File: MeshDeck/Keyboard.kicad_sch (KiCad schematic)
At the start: 12 parts, among them U8 RP2040

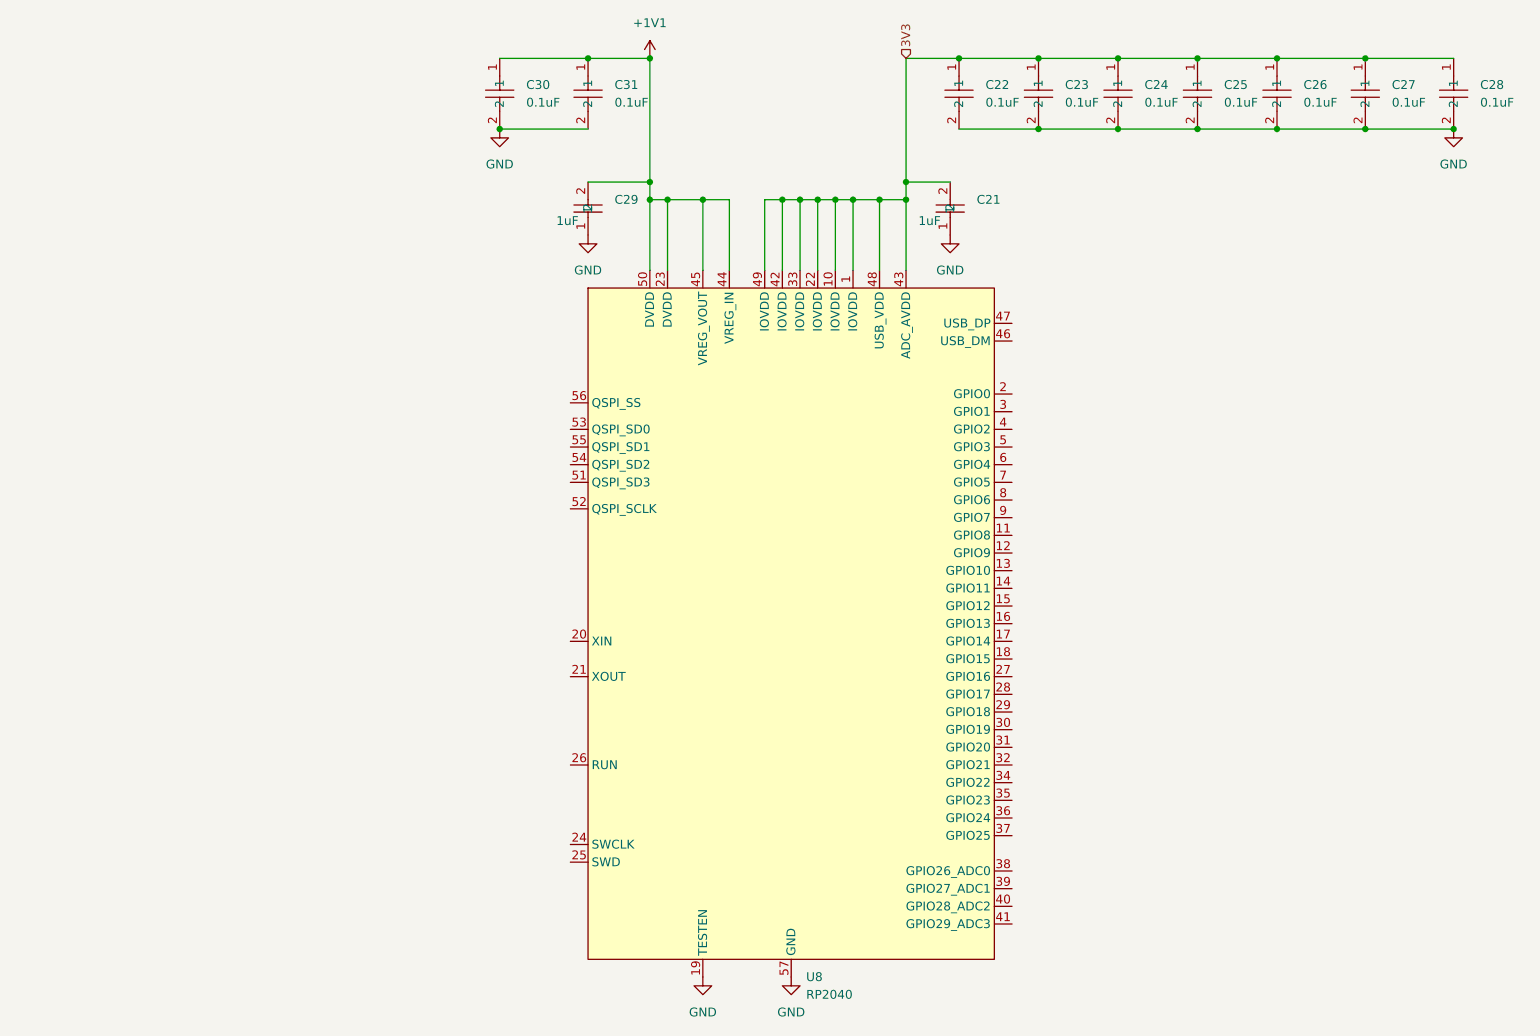
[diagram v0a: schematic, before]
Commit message: started pcb plus pin socket for expansion
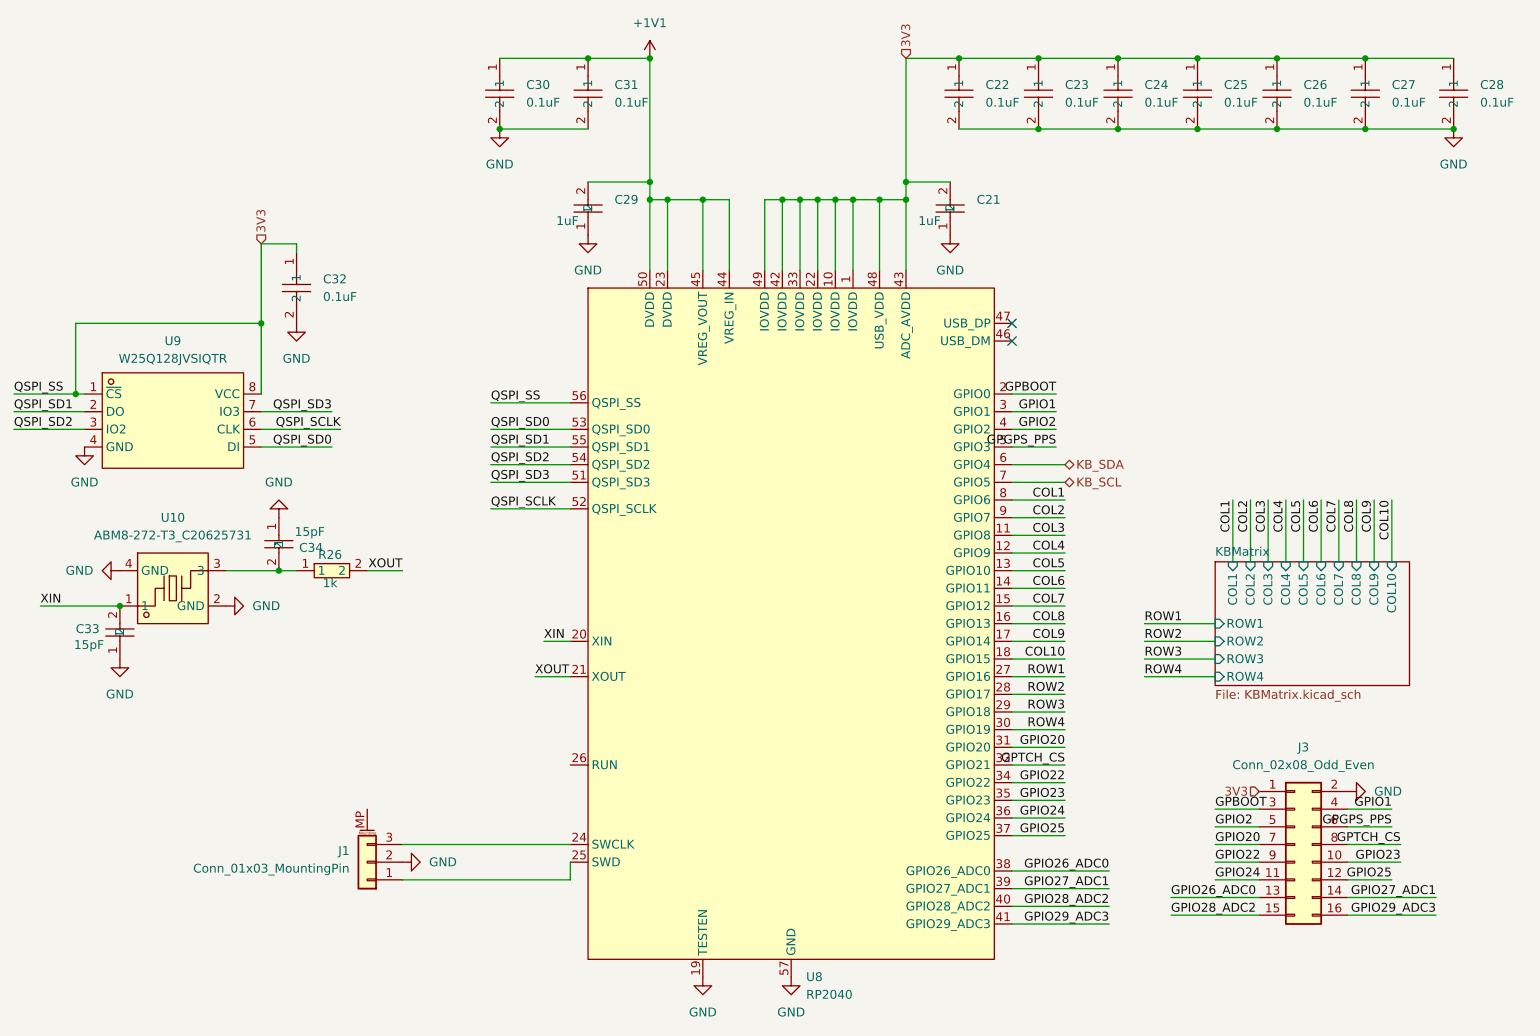
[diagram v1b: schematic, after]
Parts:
- added C32: 0.1uF, MeshDeck:C0402, symbol MeshDeck:CL05B104KO5NNNC
- added C33, C34: 15pF, MeshDeck:C0402, symbol MeshDeck:0402CG150J500NT
- added J1: Conn_01x03_MountingPin, Connector_PinHeader_2.54mm:PinHeader_1x03_P2.54mm_Horizontal, symbol Connector_Generic_MountingPin:Conn_01x03_MountingPin
- added J3: Conn_02x08_Odd_Even, Connector_PinSocket_2.54mm:PinSocket_2x08_P2.54mm_Horizontal, symbol Connector_Generic:Conn_02x08_Odd_Even
- added R26: 1k, MeshDeck:R0402, symbol MeshDeck:0402WGF1001TCE
- added U10: ABM8-272-T3_C20625731, MeshDeck:CRYSTAL-SMD_4P-L3.2-W2.5-BL, symbol MeshDeck:ABM8-272-T3_C20625731
- added U9: W25Q128JVSIQTR, MeshDeck:SOIC-8_L5.3-W5.3-P1.27-LS8.0-BL, symbol MeshDeck:W25Q128JVSIQTR
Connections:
- net 3V3: now also U8.56 (QSPI_SS), C32.1, J3.1 (Pin_1), U9.1 (~{CS}), U9.8 (VCC)
- net GND: now also C32.2, C33.1, C34.1, J1.2 (Pin_2), J3.2 (Pin_2), U10.2 (GND), U10.4 (GND), U9.4 (GND)
- net COL3: now reaches U8.11 (GPIO8)
- net COL4: now reaches U8.12 (GPIO9)
- net COL5: now reaches U8.13 (GPIO10)
- net COL6: now reaches U8.14 (GPIO11)
- net COL7: now reaches U8.15 (GPIO12)
- net COL8: now reaches U8.16 (GPIO13)
- net COL9: now reaches U8.17 (GPIO14)
- net COL10: now reaches U8.18 (GPIO15)
- net GPBOOT: now reaches U8.2 (GPIO0)
- net GPBOOT: now also J3.3 (Pin_3)
- net XIN: now reaches U8.20 (XIN)
- net XIN: now also C33.2, U10.1
- net XOUT: now reaches U8.21 (XOUT)
- net XOUT: now also R26.2
- net at U8.24 (SWCLK): now also J1.3 (Pin_3)
- net at U8.25 (SWD): now also J1.1 (Pin_1)
- net ROW1: now reaches U8.27 (GPIO16)
- net ROW2: now reaches U8.28 (GPIO17)
- net ROW3: now reaches U8.29 (GPIO18)
- net GPIO1: now reaches U8.3 (GPIO1)
- net GPIO1: now also J3.4 (Pin_4)
- net ROW4: now reaches U8.30 (GPIO19)
- net GPIO20: now reaches U8.31 (GPIO20)
- net GPIO20: now also J3.7 (Pin_7)
- net GPTCH_CS: now reaches U8.32 (GPIO21)
- net GPTCH_CS: now also J3.8 (Pin_8)
- net GPIO22: now reaches U8.34 (GPIO22)
- net GPIO22: now also J3.9 (Pin_9)
- net GPIO23: now reaches U8.35 (GPIO23)
- net GPIO23: now also J3.10 (Pin_10)
- net GPIO24: now reaches U8.36 (GPIO24)
- net GPIO24: now also J3.11 (Pin_11)
- net GPIO25: now reaches U8.37 (GPIO25)
- net GPIO25: now also J3.12 (Pin_12)
- net GPIO26_ADC0: now reaches U8.38 (GPIO26_ADC0)
- net GPIO26_ADC0: now also J3.13 (Pin_13)
- net GPIO27_ADC1: now reaches U8.39 (GPIO27_ADC1)
- net GPIO27_ADC1: now also J3.14 (Pin_14)
- net GPIO2: now reaches U8.4 (GPIO2)
- net GPIO2: now also J3.5 (Pin_5)
- net GPIO28_ADC2: now reaches U8.40 (GPIO28_ADC2)
- net GPIO28_ADC2: now also J3.15 (Pin_15)
- net GPIO29_ADC3: now reaches U8.41 (GPIO29_ADC3)
- net GPIO29_ADC3: now also J3.16 (Pin_16)
- net GPGPS_PPS: now reaches U8.5 (GPIO3)
- net GPGPS_PPS: now also J3.6 (Pin_6)
- net QSPI_SD3: now reaches U8.51 (QSPI_SD3)
- net QSPI_SD3: now also U9.7 (IO3)
- net QSPI_SCLK: now reaches U8.52 (QSPI_SCLK)
- net QSPI_SCLK: now also U9.6 (CLK)
- net QSPI_SD0: now reaches U8.53 (QSPI_SD0)
- net QSPI_SD0: now also U9.5 (DI)
- net QSPI_SD2: now reaches U8.54 (QSPI_SD2)
- net QSPI_SD2: now also U9.3 (IO2)
- net QSPI_SD1: now reaches U8.55 (QSPI_SD1)
- net QSPI_SD1: now also U9.2 (DO)
- net KB_SDA: now reaches U8.6 (GPIO4)
- net KB_SCL: now reaches U8.7 (GPIO5)
- net COL1: now reaches U8.8 (GPIO6)
- net COL2: now reaches U8.9 (GPIO7)
- new net: C34.2, R26.1, U10.3
- no-connect marks 0 -> 2
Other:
- added sheet KBMatrix (KBMatrix.kicad_sch)

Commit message: Too much routing
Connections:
- net GPBOOT renamed GPIO0
- net GPGPS_PPS renamed GPIO3
- net GPTCH_CS renamed GPIO21
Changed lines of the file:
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@@
 	(wire
 		(pts
-			(xy 170.18 119.38) (xy 162.56 119.38)
+			(xy 175.26 119.38) (xy 162.56 119.38)
 		)
 		(stroke
@@
 	(wire
 		(pts
-			(xy 168.91 73.66) (xy 162.56 73.66)
-		)
-		(stroke
-			(width 0)
-			(type default)
-		)
-	)
-	(wire
-		(pts
 			(xy 134.62 38.1) (xy 137.16 38.1)
 		)
@@
 	(wire
 		(pts
+			(xy 162.56 73.66) (xy 170.18 73.66)
+		)
+		(stroke
+			(width 0)
+			(type default)
+		)
+	)
+	(wire
+		(pts
 			(xy 200.66 27.94) (xy 213.36 27.94)
 		)
@@
 	(wire
 		(pts
-			(xy 217.17 128.27) (xy 210.82 128.27)
-		)
-		(stroke
-			(width 0)
-			(type default)
-		)
-	)
-	(wire
-		(pts
 			(xy 162.56 76.2) (xy 170.18 76.2)
 		)
@@
 		(pts
 			(xy 223.52 138.43) (xy 210.82 138.43)
+		)
+		(stroke
+			(width 0)
+			(type default)
+		)
+	)
+	(wire
+		(pts
+			(xy 210.82 128.27) (xy 215.9 128.27)
 		)
 		(stroke
@@
 		)
 	)
-	(label "GPBOOT"
+	(label "GPIO0"
 		(at 168.91 66.04 180)
 		(effects
@@
 		)
 	)
-	(label "GPTCH_CS"
-		(at 170.18 119.38 180)
+	(label "GPIO21"
+		(at 175.26 119.38 180)
 		(effects
 			(font
@@
 		)
 	)
-	(label "GPGPS_PPS"
-		(at 217.17 128.27 180)
-		(effects
-			(font
-				(size 1.27 1.27)
-			)
-			(justify right bottom)
-		)
-	)
 	(label "GPIO20"
 		(at 191.77 130.81 0)
@@
 		)
 	)
-	(label "GPBOOT"
+	(label "GPIO0"
 		(at 191.77 125.73 0)
 		(effects
@@
 		)
 	)
+	(label "GPIO3"
+		(at 170.18 73.66 180)
+		(effects
+			(font
+				(size 1.27 1.27)
+			)
+			(justify right bottom)
+		)
+	)
 	(label "COL3"
 		(at 199.39 81.28 270)
@@
 		)
 	)
-	(label "GPGPS_PPS"
-		(at 168.91 73.66 180)
-		(effects
-			(font
-				(size 1.27 1.27)
-			)
-			(justify right bottom)
-		)
-	)
 	(label "GPIO24"
 		(at 191.77 135.89 0)
@@
 		)
 	)
-	(label "GPTCH_CS"
+	(label "GPIO21"
 		(at 218.44 130.81 180)
 		(effects
@@
 		)
 	)
+	(label "GPIO3"
+		(at 215.9 128.27 180)
+		(effects
+			(font
+				(size 1.27 1.27)
+			)
+			(justify right bottom)
+		)
+	)
